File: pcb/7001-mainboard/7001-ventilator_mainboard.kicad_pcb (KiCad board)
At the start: 2 copper layers, 65 x 56.5 mm, 124 parts, among them J1 USB_B_Micro, J10 4-pin header, J11 4-pin screw terminal, J12 3-pin screw terminal, J13 2-pin screw terminal, J14 2-pin screw terminal, J2 4-pin header, J3 2-pin screw terminal, J4 DNI, J5 2-pin screw terminal, J6 5V out, J7 2-pin screw terminal, J8 3-pin screw terminal, J9 Raspberry_Pi_2_3, U1 MPRLS0001PG0000SA, U10 ABPMAND001PG2A3, U11 MPVZ5010GW6U, U12 MPVZ5010GW6U, U13 ITS4142NHUMA1, U14 ITS4142NHUMA1, U2 TPD2E2U06, U3 LPC11U37FBD48-401_, U4 MCP1825S-3302E, U5 S24SE05004PDFA_DC-DC, U6 LM2937IMP-12/NOPB, U7 AD5410AREZ, U8 MPRLS0001PG0000SA, U9 ABPMAND001PG2A3, Y1 12MHz

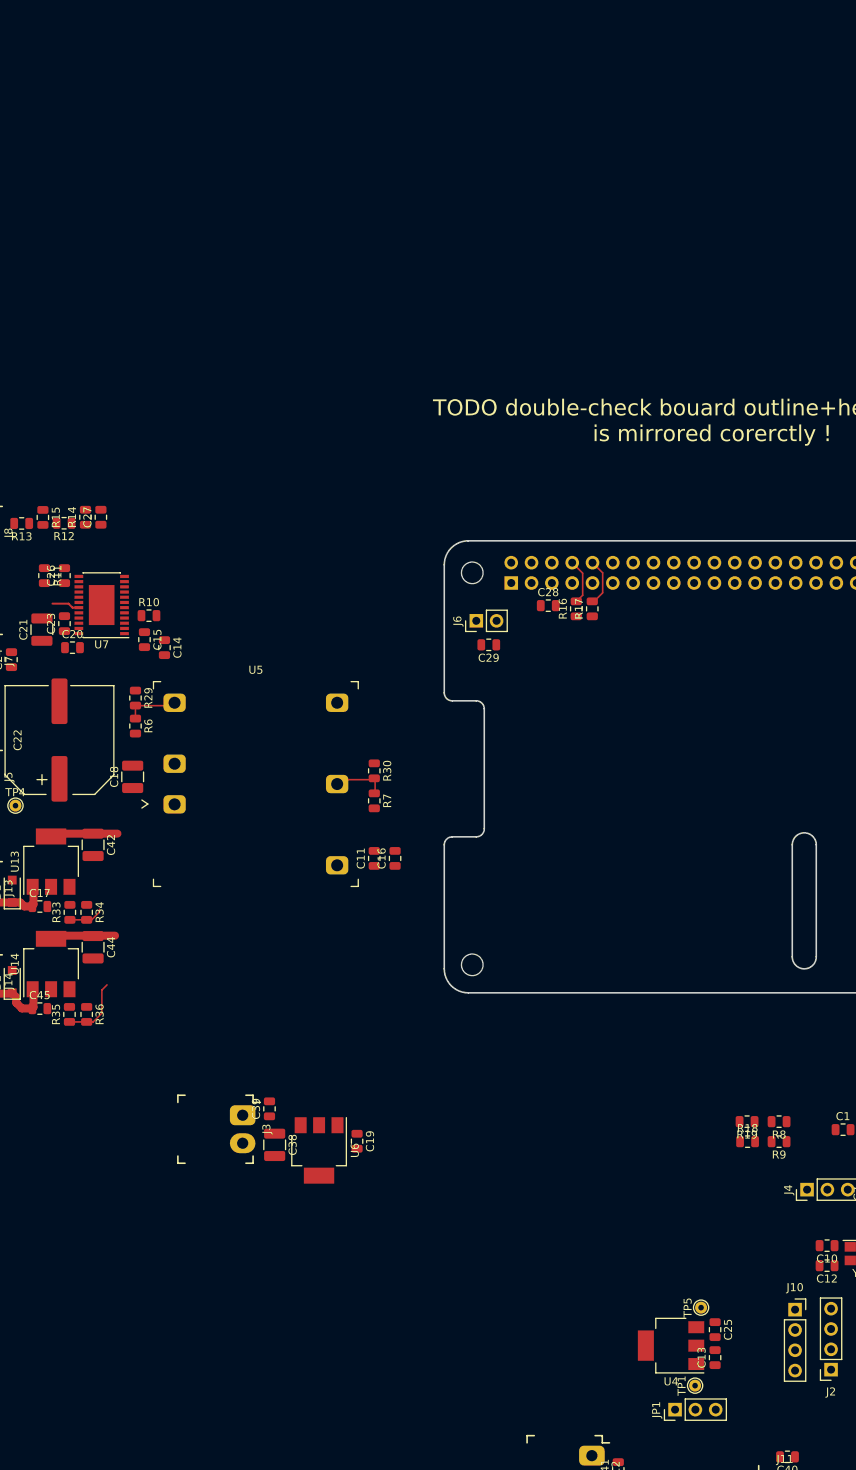
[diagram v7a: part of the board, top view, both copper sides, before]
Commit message: Sync design with BOM
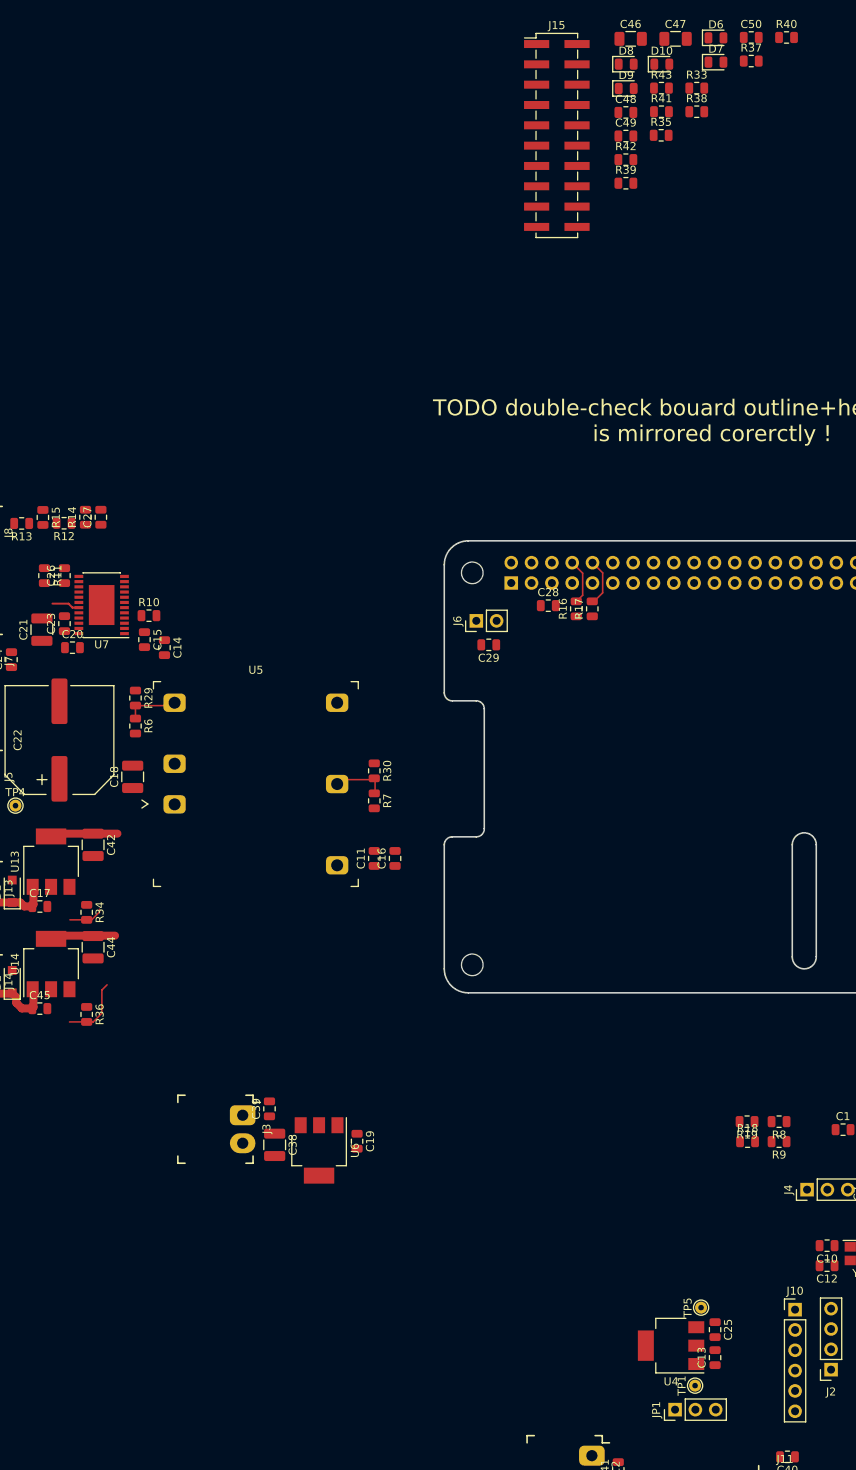
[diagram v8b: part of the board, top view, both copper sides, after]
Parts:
- added C46: 10nF 100V, Capacitor_SMD:C_1206_3216Metric, F.Cu at (123.3, 37.2)
- added C47: 10nF 100V, Capacitor_SMD:C_1206_3216Metric, F.Cu at (128.9, 37.2)
- added C48: 10nF, Capacitor_SMD:C_0805_2012Metric, F.Cu at (122.7, 46.5)
- added C49: 100nF, Capacitor_SMD:C_0805_2012Metric, F.Cu at (122.7, 49.4)
- added C50: 100nF, Capacitor_SMD:C_0805_2012Metric, F.Cu at (138.4, 37.1)
- added D10: Red, LED_SMD:LED_0805_2012Metric, F.Cu at (127.2, 40.4)
- added D6: Green, LED_SMD:LED_0805_2012Metric, F.Cu at (134.0, 37.1)
- added D7: Green, LED_SMD:LED_0805_2012Metric, F.Cu at (134.0, 40.2)
- added D8: Green, LED_SMD:LED_0805_2012Metric, F.Cu at (122.7, 40.4)
- added D9: Green, LED_SMD:LED_0805_2012Metric, F.Cu at (122.7, 43.5)
- added J15: 6-pin header, Connector_PinHeader_2.54mm:PinHeader_2x10_P2.54mm_Vertical_SMD, F.Cu at (114.1, 49.3)
- added R37: DNI, Resistor_SMD:R_0805_2012Metric, F.Cu at (138.4, 40.0)
- added R38: 3.3k, Resistor_SMD:R_0805_2012Metric, F.Cu at (131.6, 46.4)
- added R39: 10k, Resistor_SMD:R_0805_2012Metric, F.Cu at (122.7, 55.3)
- added R40: 3.3k, Resistor_SMD:R_0805_2012Metric, F.Cu at (142.8, 37.1)
- added R41: 150, Resistor_SMD:R_0805_2012Metric, F.Cu at (127.2, 46.4)
- added R42: 150, Resistor_SMD:R_0805_2012Metric, F.Cu at (122.7, 52.4)
- added R43: 150, Resistor_SMD:R_0805_2012Metric, F.Cu at (127.2, 43.4)
- J10: value 4-pin header -> 6-pin header; footprint Connector_PinSocket_2.54mm:PinSocket_1x04_P2.54mm_Vertical -> Connector_PinHeader_2.54mm:PinHeader_1x06_P2.54mm_Vertical
- R29: value 1k5 -> 3.3k
- R33: value 1k5 -> 0
- R35: value 1k5 -> 4.7k
- R6: value 68k -> 10k
- moved R35 132.5 mm to (127.1, 49.3), turned to 0 degrees
- moved R33 129.4 mm to (131.6, 43.4), turned to 0 degrees
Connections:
- J10 pad 4: +3V -> (no net)
- J2 pad 4: +3V -> (no net)
- J5 pad 1: GND -> Net-(C46-Pad2)
- J5 pad 2: +24V -> Net-(C46-Pad1)
- R31 pad 1: /A_FLOW -> GND
- R31 pad 2: Net-(J12-Pad3) -> /A_FLOW
- R32 pad 1: GND -> /A_FLOW
- R32 pad 2: /A_FLOW -> Net-(J12-Pad3)
- R33 pad 1: /switch_1_out -> /DCDC_5V
- R33 pad 2: Net-(R33-Pad2) -> +5V
- R35 pad 1: /switch_2_out -> GND
- R35 pad 2: Net-(R35-Pad2) -> /PREG_CLEAR
- U13 pad 3: Net-(R33-Pad2) -> /switch_1_out
- U14 pad 3: Net-(R35-Pad2) -> /switch_2_out
- U7 pad 13: (no net) -> Net-(R37-Pad1)
- U7 pad 22: (no net) -> Net-(C48-Pad2)
- U7 pad 6: (no net) -> /PREG_CLEAR
